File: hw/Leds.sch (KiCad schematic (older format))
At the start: 2 parts

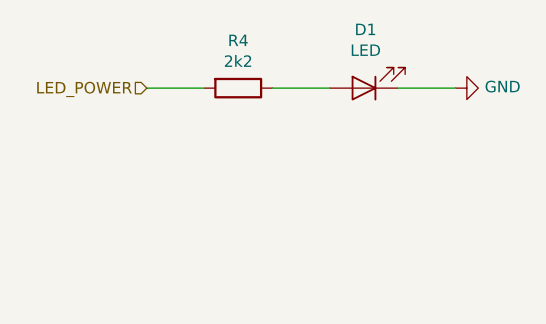
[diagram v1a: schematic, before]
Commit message: Update some packages, add 3D models
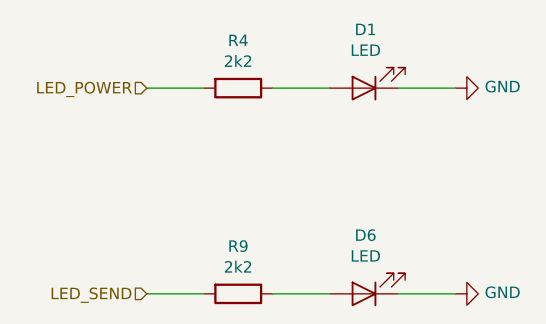
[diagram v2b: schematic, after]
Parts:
- added D6: LED, LED_SMD:LED_0603_1608Metric, symbol Device:LED
- added R9: 2k2, Resistor_SMD:R_0603_1608Metric, symbol Device:R
- D1: LCSC_ID (none) -> C72043
- R4: LCSC_ID (none) -> C4190
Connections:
- net GND: now also D6.1 (K)
- new net: D6.2 (A), R9.1
- new net LED_SEND: R9.2
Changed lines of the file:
@@
 F 2 "LED_SMD:LED_0603_1608Metric" H 5750 4000 50  0001 C CNN
 F 3 "~" H 5750 4000 50  0001 C CNN
+F 4 "C72043" H 5750 4000 50  0001 C CNN "LCSC_ID"
 	1    5750 4000
 	-1   0    0    1
@@
 F 2 "Resistor_SMD:R_0603_1608Metric" V 5130 4000 50  0001 C CNN
 F 3 "~" H 5200 4000 50  0001 C CNN
+F 4 "C4190" H 5200 4000 50  0001 C CNN "LCSC_ID"
 	1    5200 4000
 	0    1    1    0
@@
 	0    -1   -1   0
 $EndComp
+$Comp
+L Device:LED D6
+U 1 1 5F976451
+P 5750 4900
+F 0 "D6" H 5743 4645 50  0000 C CNN
+F 1 "LED" H 5743 4736 50  0000 C CNN
+F 2 "LED_SMD:LED_0603_1608Metric" H 5750 4900 50  0001 C CNN
+F 3 "~" H 5750 4900 50  0001 C CNN
+F 4 "C2286" H 5750 4900 50  0001 C CNN "LCSC_ID"
+	1    5750 4900
+	-1   0    0    1
+$EndComp
+Wire Wire Line
+	5600 4900 5350 4900
+$Comp
+L Device:R R9
+U 1 1 5F976459
+P 5200 4900
+F 0 "R9" V 4993 4900 50  0000 C CNN
+F 1 "2k2" V 5084 4900 50  0000 C CNN
+F 2 "Resistor_SMD:R_0603_1608Metric" V 5130 4900 50  0001 C CNN
+F 3 "~" H 5200 4900 50  0001 C CNN
+F 4 "C4190" H 5200 4900 50  0001 C CNN "LCSC_ID"
+	1    5200 4900
+	0    1    1    0
+$EndComp
+Wire Wire Line
+	5050 4900 4800 4900
+Text HLabel 4800 4900 0    50   Input ~ 0
+LED_SEND
+Wire Wire Line
+	5900 4900 6150 4900
+$Comp
+L power:GND #PWR0123
+U 1 1 5F976462
+P 6150 4900
+F 0 "#PWR0123" H 6150 4650 50  0001 C CNN
+F 1 "GND" V 6155 4772 50  0000 R CNN
+F 2 "" H 6150 4900 50  0001 C CNN
+F 3 "" H 6150 4900 50  0001 C CNN
+	1    6150 4900
+	0    -1   -1   0
+$EndComp
